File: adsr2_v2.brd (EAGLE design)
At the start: 99.4 x 29.2 mm, 55 parts, among them IC1 LM324D, IC2 4052D, SW1_TIME TL2285 L, SW2_TRIG TL2285 L, T1 BC847, T2 BC857, T3 BC857, T4 BC847, T5 BC857

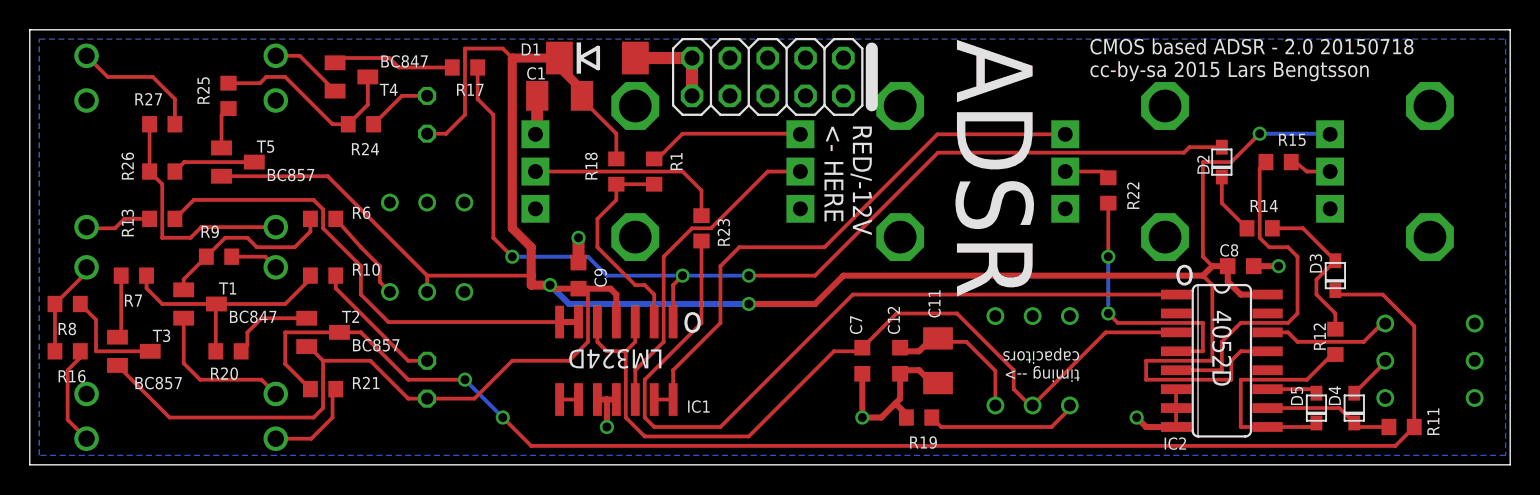
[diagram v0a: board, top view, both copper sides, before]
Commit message: Renamed comparator output net to "peak". Minor routing fixes on PCB.
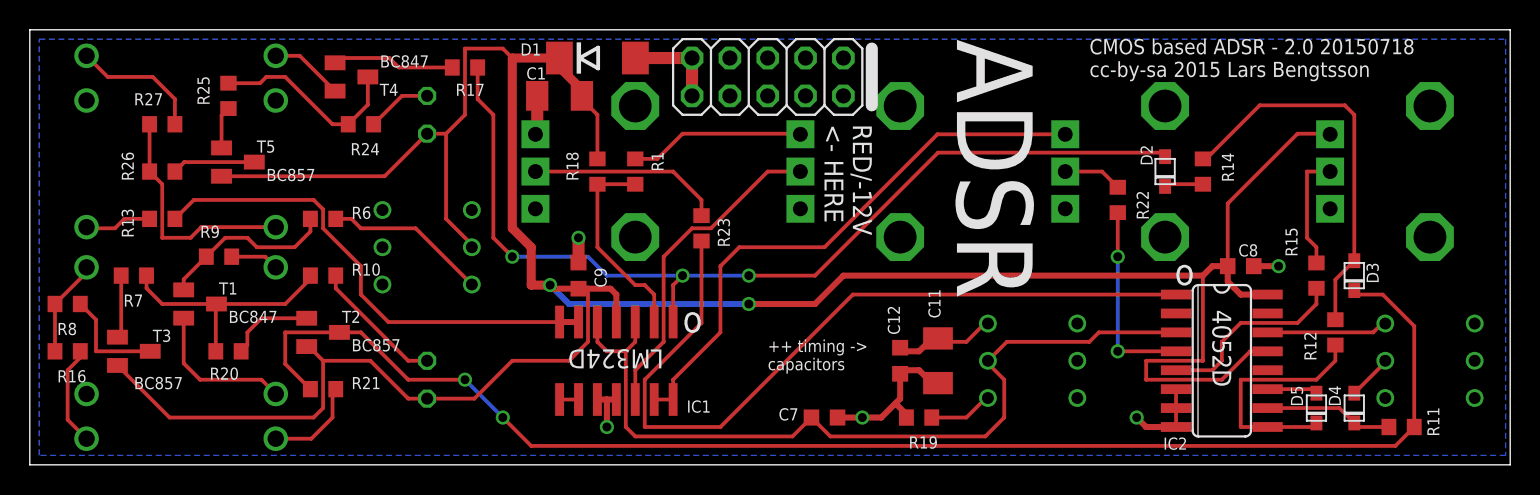
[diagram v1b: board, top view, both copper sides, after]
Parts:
- moved R15 8.03 mm to (86.4, 23.5), turned to 270 degrees
- moved R14 5.39 mm to (78.7, 30.5), turned to 90 degrees
- moved C7 4.58 mm to (53.3, 14.0), turned to 0 degrees
- moved D2 3.86 mm to (76.2, 30.5)
- moved D3 1.27 mm to (88.9, 23.5)
- moved R1 1.27 mm to (40.6, 30.5)
- moved R18 1.27 mm to (38.1, 30.5)
- moved R22 0.90 mm to (73.0, 28.6)
- moved R12 0.63 mm to (87.6, 19.7)
- turned SW1_TIME to 90 degrees
- turned SW_MANUAL to 90 degrees
- renumbered AT_TRIG to PEAK_OUT
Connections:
- net ATTACK_DONE renamed PEAK
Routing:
- net N$17: track 10.8 -> 26.2 mm
- net N$10: track 23.0 -> 13.1 mm
- net +12V: track 204.0 -> 196.9 mm, vias 3 -> 2
- net N$18: track 10.3 -> 4.31 mm
- net N$28: track 3.12 -> 7.95 mm
- net N$4: track 6.35 -> 11.0 mm
- net N$6: track 17.7 -> 13.2 mm
- net PEAK: track 68.8 -> 64.9 mm
- net N$16: track 10.1 -> 6.95 mm
- net N$29: track 4.15 -> 2.60 mm
- net GATE: track 97.0 -> 95.8 mm
- net N$26: track 10.5 -> 11.8 mm
- net GND: track 63.4 -> 62.2 mm
- net N$15: track 3.06 -> 3.96 mm
- net MUXB: track 15.4 -> 16.3 mm
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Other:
- board text added: "++ timing -> capacitors"
- board text removed: "timing --> capacitors"

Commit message: Changed R1 to 1k.
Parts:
- R1: value 470 -> 1k
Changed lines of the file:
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@@
 <attribute name="NAME" x="0.6096" y="37.7952" size="1.27" layer="22" rot="MR180"/>
 </element>
-<element name="R1" library="rcl" package="R0603" value="470" x="40.64" y="30.48" smashed="yes" rot="R90">
+<element name="R1" library="rcl" package="R0603" value="1k" x="40.64" y="30.48" smashed="yes" rot="R90">
 <attribute name="NAME" x="42.545" y="30.48" size="0.8128" layer="25" font="vector" rot="R90"/>
 </element>

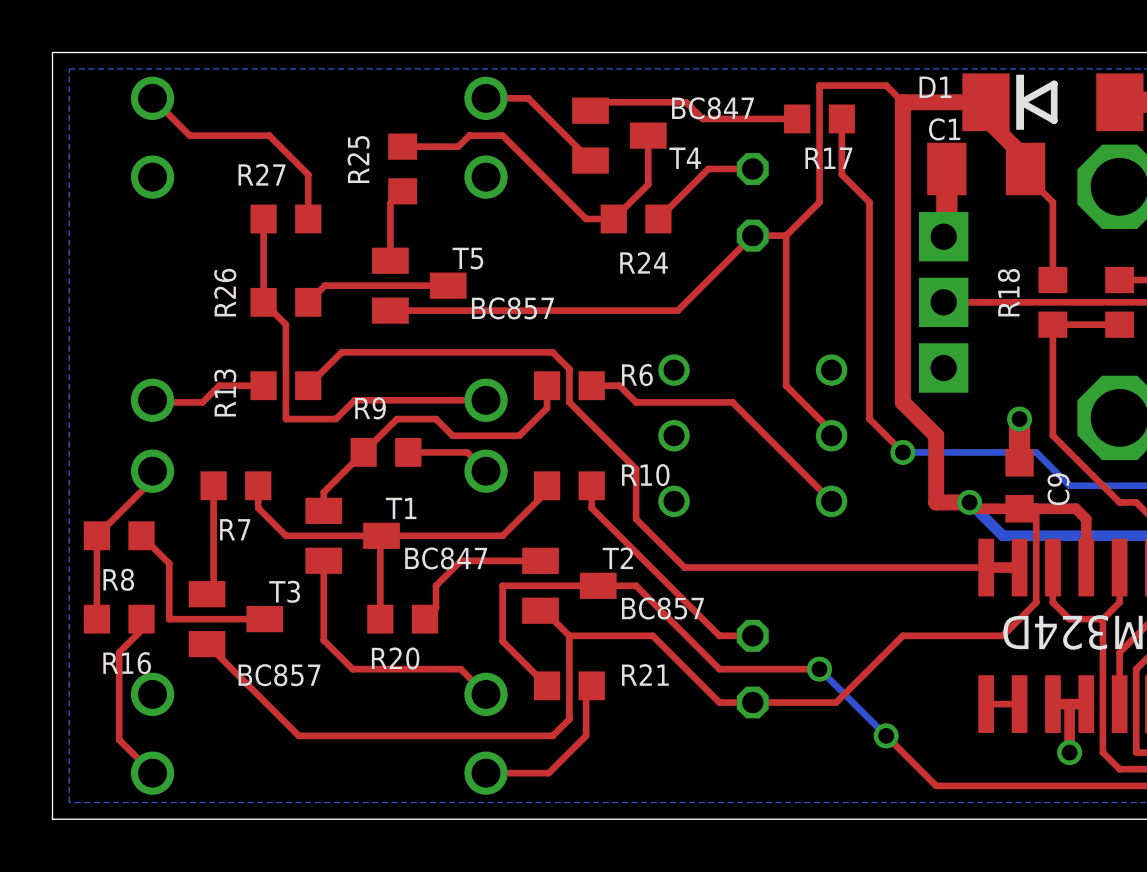
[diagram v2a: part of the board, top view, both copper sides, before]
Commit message: Changed LEDs to 5mm footprint. Moved T3 and surrounding resistors a bit.
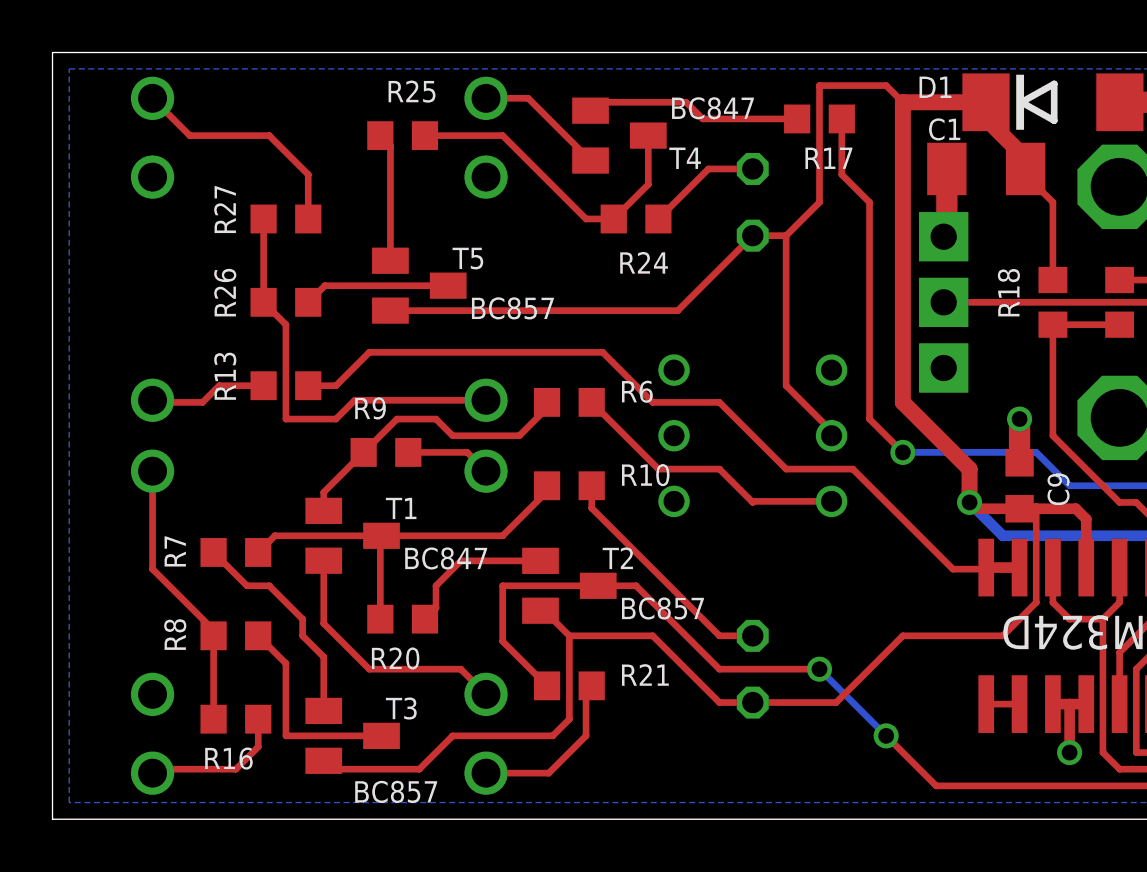
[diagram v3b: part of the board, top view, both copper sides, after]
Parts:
- LED1: value AT_TRIG_LED -> PEAK_LED; device led:LED3MM -> led:LED5MM
- LED4: device led:LED3MM -> led:LED5MM
- moved T3 6.29 mm to (11.4, 14.0)
- moved R16 5.85 mm to (6.99, 14.6)
- moved R8 5.85 mm to (6.99, 17.8)
- moved R7 2.54 mm to (6.99, 21.0)
- moved R25 1.27 mm to (13.3, 36.8), turned to 180 degrees
- moved R6 0.63 mm to (19.7, 26.7)
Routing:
- net +12V: track 196.9 -> 190.9 mm
- net N$8: track 4.23 -> 8.27 mm
- net N$13: track 6.51 -> 10.4 mm
- net N$33: track 2.84 -> 4.92 mm
- net N$12: track 32.9 -> 31.1 mm
- net GND: track 62.2 -> 60.5 mm
- net N$30: track 13.2 -> 12.2 mm
- net GATE_IN: track 16.4 -> 15.4 mm
- net N$9: track 7.25 -> 7.89 mm
- net N$21: track 11.9 -> 11.3 mm

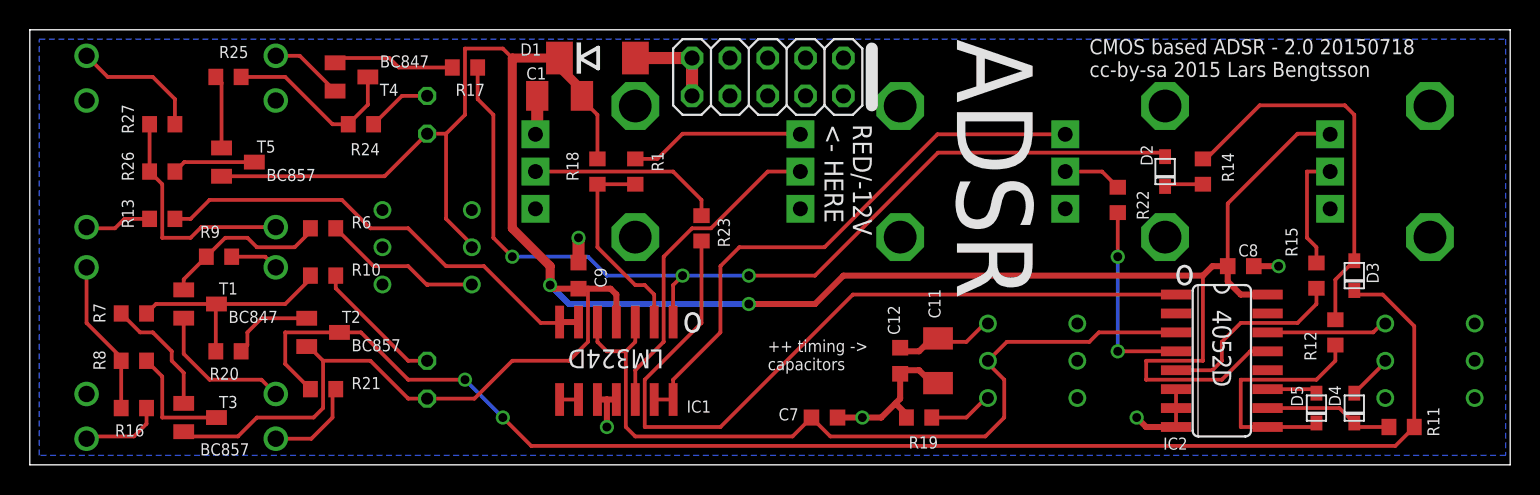
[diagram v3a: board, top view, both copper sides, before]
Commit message: Added circuit to make sure peak output pulse has at least a few ms duration. Changed peak output to behave like decay+sustain gate rather than just "attack done" trigger output.
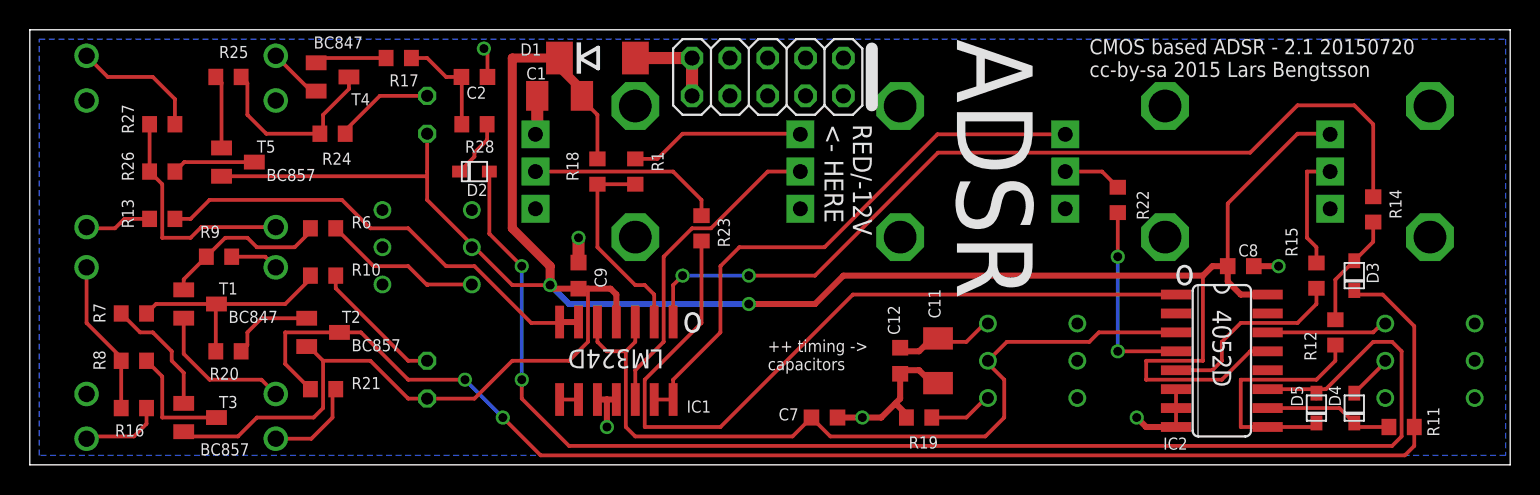
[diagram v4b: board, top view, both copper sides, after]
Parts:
- added C2: 4n7, rcl:C0603K
- added R28: 1k, rcl:R0603
- moved D2 46.4 mm to (29.8, 30.5), turned to 180 degrees
- moved R14 11.7 mm to (90.2, 27.9), turned to 270 degrees
- moved R17 4.49 mm to (24.8, 38.1)
- moved R24 2.01 mm to (20.3, 33.0)
- moved T4 1.27 mm to (20.3, 36.8)
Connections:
- removed net N$29: D2.C, R14.1
- new net N$14: D2.C, R28.2
- new net N$20: C2.1, R17.2, R28.1
- net DEC_SUST: now also D2.A
- net GND: now also C2.2
- net PEAK: now also R14.1; no longer D2.A, R17.2
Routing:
- net DEC_SUST: track 3.39 -> 93.8 mm, vias 0 -> 2
- net N$17: track 26.2 -> 7.61 mm
- net N$20: track 0.00 -> 7.24 mm
- net +12V: track 190.9 -> 185.7 mm
- net PEAK: track 64.9 -> 59.9 mm, vias 3 -> 2
- net N$14: track 0.00 -> 3.94 mm
- net N$19: track 8.27 -> 4.83 mm
- net N$29: track 2.60 -> 0.00 mm
- net N$31: track 4.38 -> 6.68 mm
- net GATE: track 95.8 -> 97.0 mm
- net GND: track 60.5 -> 61.3 mm, vias 5 -> 6
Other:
- board text added: "CMOS based ADSR - 2.1 20150720 cc-by-sa 2015 Lars Bengtsson"
- board text removed: "CMOS based ADSR - 2.0 20150718 cc-by-sa 2015 Lars Bengtsson"

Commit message: Small routing adjustments.
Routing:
- net N$12: track 31.1 -> 35.7 mm
- net +12V: track 185.7 -> 186.7 mm
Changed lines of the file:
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@@
 <text x="49.53" y="17.145" size="0.8128" layer="25" font="vector" rot="SR0">++ timing -&gt;
 capacitors</text>
-<text x="56.515" y="15.24" size="6.4516" layer="26" font="vector" rot="SMR0">ADSR</text>
+<text x="35.56" y="21.59" size="6.4516" layer="26" font="vector" rot="SMR180">ADSR</text>
 </plain>
 <attributes>
@@
 <via x="34.925" y="22.86" extent="1-16" drill="0.6" shape="square"/>
 <wire x1="34.925" y1="22.86" x2="36.195" y2="21.59" width="0.4064" layer="16"/>
-<wire x1="36.195" y1="21.59" x2="48.26" y2="21.59" width="0.4064" layer="16"/>
-<via x="48.26" y="21.59" extent="1-16" drill="0.6" shape="square"/>
+<wire x1="36.195" y1="21.59" x2="46.99" y2="21.59" width="0.4064" layer="16"/>
+<via x="46.99" y="21.59" extent="1-16" drill="0.6" shape="square"/>
 <wire x1="34.925" y1="22.86" x2="34.925" y2="24.13" width="0.6096" layer="1"/>
 <wire x1="36.83" y1="22.62" x2="35.165" y2="22.62" width="0.4064" layer="1"/>
@@
 <wire x1="39.37" y1="22.225" x2="39.37" y2="20.38" width="0.4064" layer="1"/>
 <wire x1="34.925" y1="24.13" x2="32.385" y2="26.67" width="0.6096" layer="1"/>
-<wire x1="32.385" y1="26.67" x2="32.385" y2="38.1" width="0.6096" layer="1"/>
+<wire x1="32.385" y1="26.67" x2="32.385" y2="34.925" width="0.6096" layer="1"/>
 <contactref element="SW_MANUAL" pad="5"/>
+<wire x1="32.385" y1="34.925" x2="32.385" y2="37.465" width="0.6096" layer="1"/>
 <wire x1="18.585" y1="18.735" x2="18.73" y2="18.735" width="0.254" layer="1"/>
 <wire x1="18.73" y1="18.735" x2="19.685" y2="17.78" width="0.254" layer="1"/>
@@
 <wire x1="36.195" y1="17.78" x2="37.465" y2="19.05" width="0.254" layer="1"/>
 <wire x1="37.465" y1="19.05" x2="37.465" y2="22.62" width="0.254" layer="1"/>
-<wire x1="32.385" y1="38.1" x2="35.55" y2="38.1" width="0.6096" layer="1"/>
+<wire x1="32.385" y1="37.465" x2="33.02" y2="38.1" width="0.6096" layer="1"/>
+<wire x1="33.02" y1="38.1" x2="35.55" y2="38.1" width="0.6096" layer="1"/>
 <wire x1="35.55" y1="38.1" x2="35.55" y2="37.475" width="0.6096" layer="1"/>
 <wire x1="35.55" y1="37.475" x2="36.83" y2="36.195" width="0.6096" layer="1"/>
@@
 <wire x1="38.1" y1="34.29" x2="38.1" y2="31.33" width="0.254" layer="1"/>
 <contactref element="IC2" pad="16"/>
-<wire x1="48.26" y1="21.59" x2="52.705" y2="21.59" width="0.4064" layer="1"/>
+<wire x1="46.99" y1="21.59" x2="52.705" y2="21.59" width="0.4064" layer="1"/>
 <wire x1="52.705" y1="21.59" x2="54.61" y2="23.495" width="0.4064" layer="1"/>
 <wire x1="54.61" y1="23.495" x2="78.74" y2="23.495" width="0.4064" layer="1"/>
@@
 <wire x1="29.67" y1="25.575" x2="26.67" y2="28.575" width="0.254" layer="1"/>
 <wire x1="26.67" y1="28.575" x2="26.67" y2="30.165" width="0.254" layer="1"/>
-<wire x1="26.67" y1="30.48" x2="26.67" y2="33.02" width="0.254" layer="1"/>
+<wire x1="26.67" y1="30.165" x2="26.67" y2="33.02" width="0.254" layer="1"/>
 <wire x1="19.05" y1="13.97" x2="15.24" y2="13.97" width="0.254" layer="1"/>
 <wire x1="15.24" y1="13.97" x2="13.97" y2="12.7" width="0.254" layer="1"/>
 <wire x1="13.97" y1="12.7" x2="10.65" y2="12.7" width="0.254" layer="1"/>
 <wire x1="10.65" y1="12.7" x2="10.33" y2="13.02" width="0.254" layer="1"/>
-<wire x1="29.67" y1="25.575" x2="32.385" y2="22.86" width="0.254" layer="1"/>
-<wire x1="32.385" y1="22.86" x2="34.925" y2="22.86" width="0.254" layer="1"/>
-<wire x1="26.67" y1="30.165" x2="26.67" y2="30.48" width="0.254" layer="1"/>
+<wire x1="32.385" y1="34.925" x2="30.48" y2="34.925" width="0.254" layer="1"/>
+<wire x1="30.48" y1="34.925" x2="29.845" y2="34.29" width="0.254" layer="1"/>
+<wire x1="29.845" y1="34.29" x2="29.845" y2="33.02" width="0.254" layer="1"/>
+<wire x1="29.845" y1="33.02" x2="29.21" y2="32.385" width="0.254" layer="1"/>
+<wire x1="29.21" y1="32.385" x2="27.305" y2="32.385" width="0.254" layer="1"/>
+<wire x1="27.305" y1="32.385" x2="26.67" y2="33.02" width="0.254" layer="1"/>
 </signal>
 <signal name="SUST_LEVEL">
@@
 <wire x1="69.5" y1="32.98" x2="60.92" y2="32.98" width="0.254" layer="1"/>
 <wire x1="60.92" y1="32.98" x2="53.34" y2="25.4" width="0.254" layer="1"/>
-<wire x1="53.34" y1="25.4" x2="47.625" y2="25.4" width="0.254" layer="1"/>
-<wire x1="47.625" y1="25.4" x2="46.355" y2="24.13" width="0.254" layer="1"/>
-<wire x1="46.355" y1="24.13" x2="46.355" y2="19.685" width="0.254" layer="1"/>
-<wire x1="46.355" y1="19.685" x2="43.18" y2="16.51" width="0.254" layer="1"/>
+<wire x1="53.34" y1="25.4" x2="46.99" y2="25.4" width="0.254" layer="1"/>
+<wire x1="46.99" y1="25.4" x2="45.72" y2="24.13" width="0.254" layer="1"/>
+<wire x1="45.72" y1="24.13" x2="45.72" y2="19.05" width="0.254" layer="1"/>
+<wire x1="45.72" y1="19.05" x2="43.18" y2="16.51" width="0.254" layer="1"/>
 <wire x1="43.18" y1="16.51" x2="43.18" y2="15.18" width="0.254" layer="1"/>
 </signal>
@@
 <wire x1="30.845" y1="30.48" x2="30.845" y2="26.305" width="0.254" layer="1"/>
 <wire x1="30.845" y1="26.305" x2="33.02" y2="24.13" width="0.254" layer="1"/>
-<via x="33.02" y="24.13" extent="1-16" drill="0.6" shape="square"/>
-<wire x1="33.02" y1="24.13" x2="33.02" y2="16.51" width="0.254" layer="16"/>
+<wire x1="33.02" y1="24.13" x2="33.02" y2="19.685" width="0.254" layer="1"/>
+<via x="33.02" y="19.685" extent="1-16" drill="0.6" shape="square"/>
+<wire x1="33.02" y1="19.685" x2="33.02" y2="16.51" width="0.254" layer="16"/>
 <wire x1="91.44" y1="12.065" x2="92.075" y2="12.7" width="0.254" layer="1"/>
 <wire x1="92.075" y1="12.7" x2="92.075" y2="18.415" width="0.254" layer="1"/>
@@
 <wire x1="22.86" y1="26.67" x2="25.4" y2="26.67" width="0.254" layer="1"/>
 <wire x1="25.4" y1="26.67" x2="27.94" y2="24.13" width="0.254" layer="1"/>
-<wire x1="27.94" y1="24.13" x2="29.845" y2="24.13" width="0.254" layer="1"/>
-<wire x1="29.845" y1="24.13" x2="33.655" y2="20.32" width="0.254" layer="1"/>
-<wire x1="33.655" y1="20.32" x2="35.5" y2="20.32" width="0.254" layer="1"/>
+<wire x1="27.94" y1="24.13" x2="30.48" y2="24.13" width="0.254" layer="1"/>
 <wire x1="35.5" y1="20.32" x2="35.56" y2="20.38" width="0.254" layer="1"/>
+<wire x1="30.48" y1="24.13" x2="31.115" y2="23.495" width="0.254" layer="1"/>
+<wire x1="31.115" y1="23.495" x2="31.115" y2="19.685" width="0.254" layer="1"/>
+<wire x1="31.115" y1="19.685" x2="32.385" y2="18.415" width="0.254" layer="1"/>
+<wire x1="32.385" y1="18.415" x2="34.925" y2="18.415" width="0.254" layer="1"/>
+<wire x1="34.925" y1="18.415" x2="35.56" y2="19.05" width="0.254" layer="1"/>
+<wire x1="35.56" y1="19.05" x2="35.56" y2="20.38" width="0.254" layer="1"/>
 </signal>
 <signal name="N$11">
@@
 <signal name="PEAK">
 <contactref element="IC1" pad="1"/>
-<wire x1="52.705" y1="23.495" x2="48.26" y2="23.495" width="0.254" layer="1"/>
-<via x="48.26" y="23.495" extent="1-16" drill="0.6" shape="square"/>
-<wire x1="48.26" y1="23.495" x2="43.815" y2="23.495" width="0.254" layer="16"/>
+<wire x1="52.705" y1="23.495" x2="46.99" y2="23.495" width="0.254" layer="1"/>
+<via x="46.99" y="23.495" extent="1-16" drill="0.6" shape="square"/>
+<wire x1="46.99" y1="23.495" x2="43.815" y2="23.495" width="0.254" layer="16"/>
 <via x="43.815" y="23.495" extent="1-16" drill="0.6" shape="square"/>
 <wire x1="43.815" y1="23.495" x2="43.18" y2="22.86" width="0.254" layer="1"/>
